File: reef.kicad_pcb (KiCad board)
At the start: 2 copper layers, 87 parts, among them J1 nice!view sockets, J2 battery connector, SW0 B3U-1000P[], SW1 PCM12SMTR, U1 nice_nano, U2 TRRS, U3 TRRS

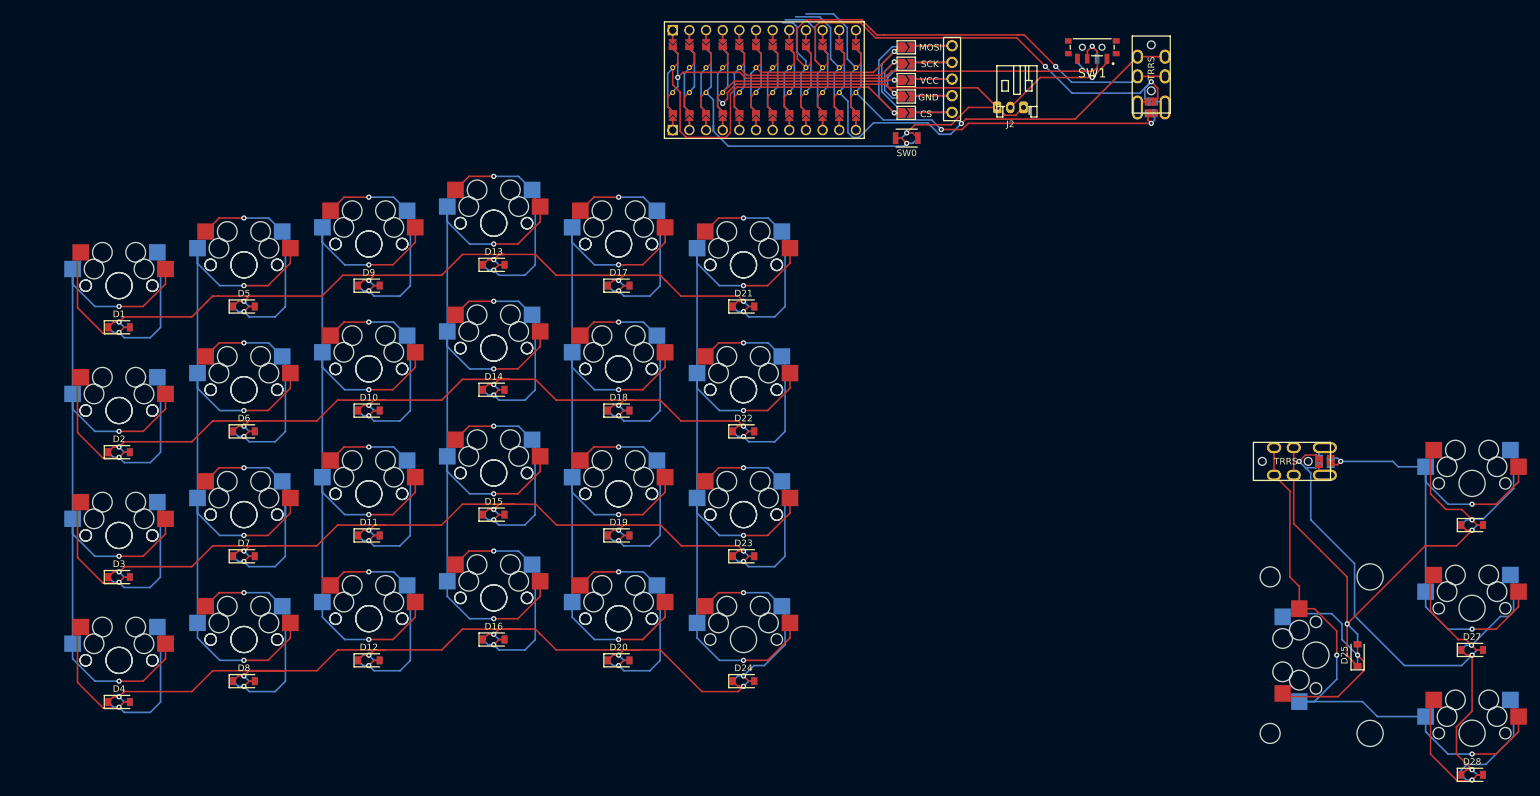
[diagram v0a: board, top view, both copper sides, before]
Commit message: Layout
arranged everything in rough layout of final board
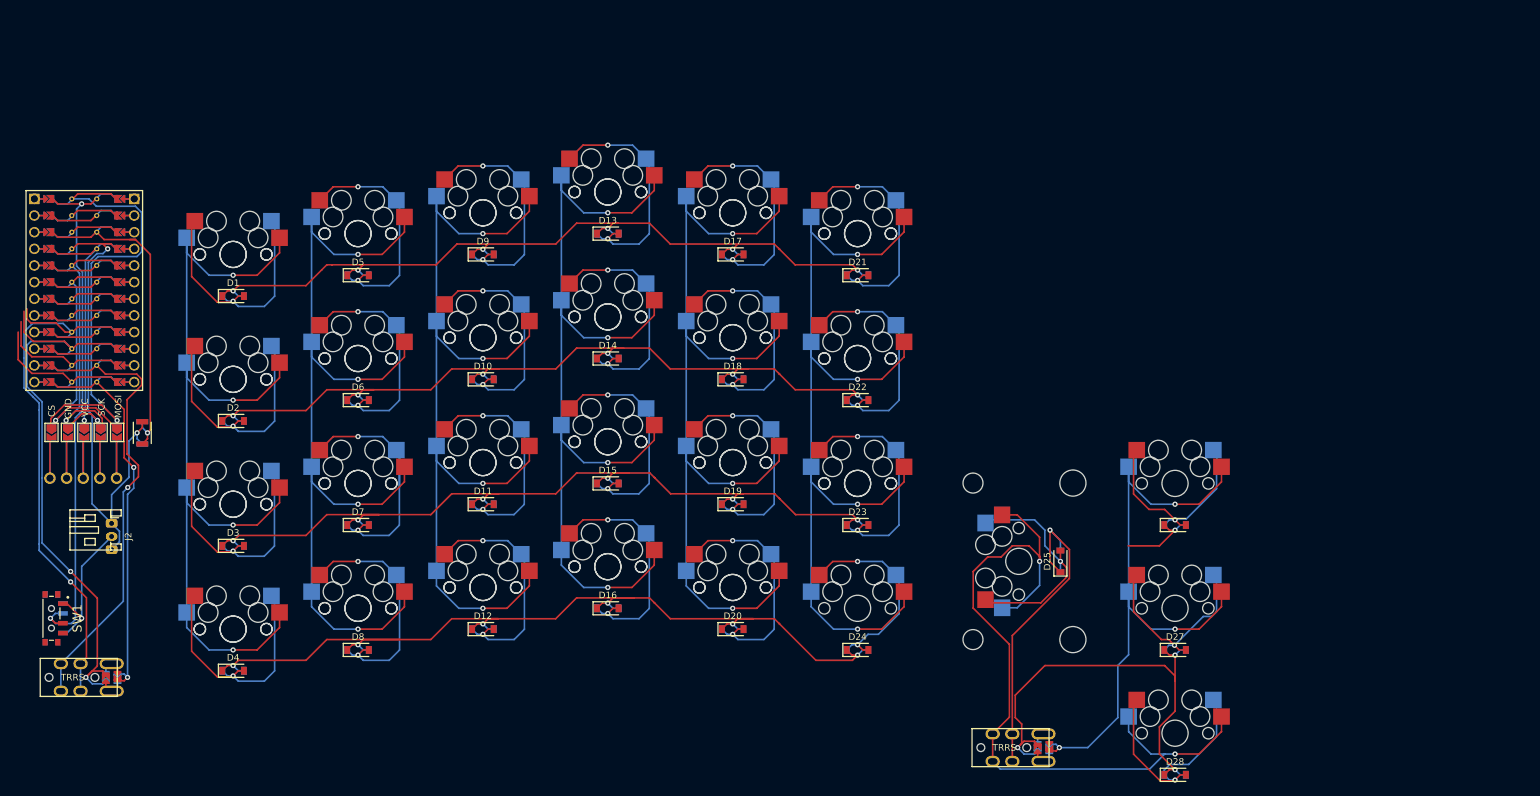
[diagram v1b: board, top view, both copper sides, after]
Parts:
- Display1, J2, SW1, U1, U2: moved to B.Cu
- J1, SW0: moved to F.Cu
- moved U2 195.9 mm to (34.7, 128.8), turned to -90 degrees
- moved SW1 183.3 mm to (34.9, 119.8), turned to 90 degrees
- moved Display1 165.3 mm to (41.3, 112.9), turned to 0 degrees
- moved J2 155.9 mm to (42.7, 107.3), turned to 90 degrees
- moved J1 136.1 mm to (41.6, 91.3), turned to 180 degrees
- moved SW0 125.0 mm to (50.4, 91.5), turned to -90 degrees
- moved U1 108.6 mm to (41.5, 69.8), turned to -90 degrees
- moved U3 61.2 mm to (176.8, 139.5)
- moved D25 47.5 mm to (190.4, 111.1)
- moved MX25 47.5 mm to (184.1, 111.1)
- moved D26 45.3 mm to (207.9, 105.6)
- moved D27 45.3 mm to (207.9, 124.6)
- moved D28 45.3 mm to (207.9, 143.7)
- moved MX26 45.3 mm to (207.9, 99.2)
- moved MX27 45.3 mm to (207.9, 118.3)
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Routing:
- net thc_6: track 89.6 -> 116.4 mm
- net thc_7: track 80.2 -> 97.6 mm
- net thr_1: track 82.0 -> 71.0 mm
- net thr_0: track 70.0 -> 63.0 mm

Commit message: Traces Routed
all traces should now be fully routed
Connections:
- U1 pad 10: row_1 -> row_2
- U1 pad 11: row_2 -> row_1
- U1 pad 12: row_3 -> row_0
- U1 pad 15: col_5 -> col_0
- U1 pad 16: col_4 -> col_1
- U1 pad 17: col_3 -> col_2
- U1 pad 18: col_2 -> col_3
- U1 pad 19: col_1 -> col_4
- U1 pad 20: col_0 -> col_5
- U1 pad 9: row_0 -> row_3
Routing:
- net col_5: track 143.6 -> 277.3 mm
- net col_4: track 143.6 -> 258.2 mm
- net row_3: track 158.9 -> 270.7 mm
- net row_2: track 151.0 -> 248.3 mm
- net col_3: track 143.6 -> 232.9 mm
- net row_1: track 219.4 -> 297.8 mm
- net col_2: track 143.6 -> 215.3 mm
- net row_0: track 208.4 -> 270.0 mm, vias 7 -> 6
- net col_1: track 143.6 -> 196.2 mm
- net col_0: track 143.6 -> 195.2 mm

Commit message: Teardrops and Fillets
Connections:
- Display1 pad 1: (no net) -> disp_1
- Display1 pad 2: (no net) -> disp_2
- Display1 pad 3: (no net) -> disp_3
- Display1 pad 4: (no net) -> disp_4
- Display1 pad 5: (no net) -> disp_5
- J1 pad 10: (no net) -> disp_1
- J1 pad 6: (no net) -> disp_1
- J1 pad 7: (no net) -> disp_2
- J1 pad 8: (no net) -> disp_3
- J1 pad 9: (no net) -> disp_4
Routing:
- net (no net): track 63.3 -> 0.00 mm
- net disp_1: track 0.00 -> 12.7 mm
- net disp_2: track 0.00 -> 12.7 mm
- net disp_3: track 0.00 -> 12.7 mm
- net disp_4: track 0.00 -> 12.6 mm
- net disp_5: track 0.00 -> 12.6 mm
- net row_1: track 297.8 -> 295.9 mm
- net row_3: track 270.7 -> 269.1 mm
- net row_0: track 270.0 -> 268.4 mm
- net row_2: track 248.3 -> 246.8 mm
- net col_5: track 277.3 -> 276.1 mm
- net col_4: track 258.2 -> 257.1 mm
- net col_0: track 195.2 -> 194.2 mm
- net col_3: track 232.9 -> 231.9 mm
- net col_2: track 215.3 -> 214.4 mm
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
